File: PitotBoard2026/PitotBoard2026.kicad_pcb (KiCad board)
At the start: 2 copper layers, 50.2 x 41.5 mm, 65 parts, among them J1 RJ25, J2 ICSP(, J3 Conn_01x04_Socket, J4 Conn_01x04_Pin, J5 Conn_01x04_Socket, J6 Conn_01x04_Pin, SW1 RST, U1 ATmega328PB-A, U10 MCP25625-x-SS, U11 FXMA2102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

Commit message: Add files via upload
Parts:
- added ? (x2): , , F.Cu at (180.5, 141.7)
- added ? (x2): , , F.Cu at (180.5, 140.9)
- added ?: , , F.Cu at (145.9, 141.3)
- added ? (x2): , , F.Cu at (145.9, 139.7)
- added ?: , , F.Cu at (180.5, 142.5)
- added ? (x2): , , F.Cu at (145.9, 140.5)
- added G***: LOGO, KUBTSS:CYGNUS, F.Cu at (150.5, 140.1)
- added G***: LOGO, KUBTSS:Lba, F.Cu at (150.7, 137.1)
- added REF**: MountingHole_2.1mm, MountingHole:MountingHole_2.1mm, F.Cu at (145.9, 141.3)
- added REF**: MountingHole_2.1mm, MountingHole:MountingHole_2.1mm, F.Cu at (180.5, 142.5)
- moved J6 56.6 mm to (182.6, 137.0)
- moved C27 56.6 mm to (186.2, 139.9)
- moved U3 56.6 mm to (186.4, 142.4)
- moved C14 3.54 mm to (135.3, 134.5)
- moved J4 3.54 mm to (135.1, 129.0)
- moved C15 3.54 mm to (139.4, 139.1)
- moved REF** 3.54 mm to (143.3, 140.5)
- moved REF** 3.54 mm to (135.0, 140.5)
- moved U7 3.54 mm to (138.8, 134.6)
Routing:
- net GND2: track 26.9 -> 35.6 mm, vias 2 -> 8
- net GND: track 155.3 -> 159.5 mm, vias 35 -> 40
- net GND1: vias 3 -> 5
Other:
- board size 50.2 x 41.5 mm -> 59.7 x 40.2 mm

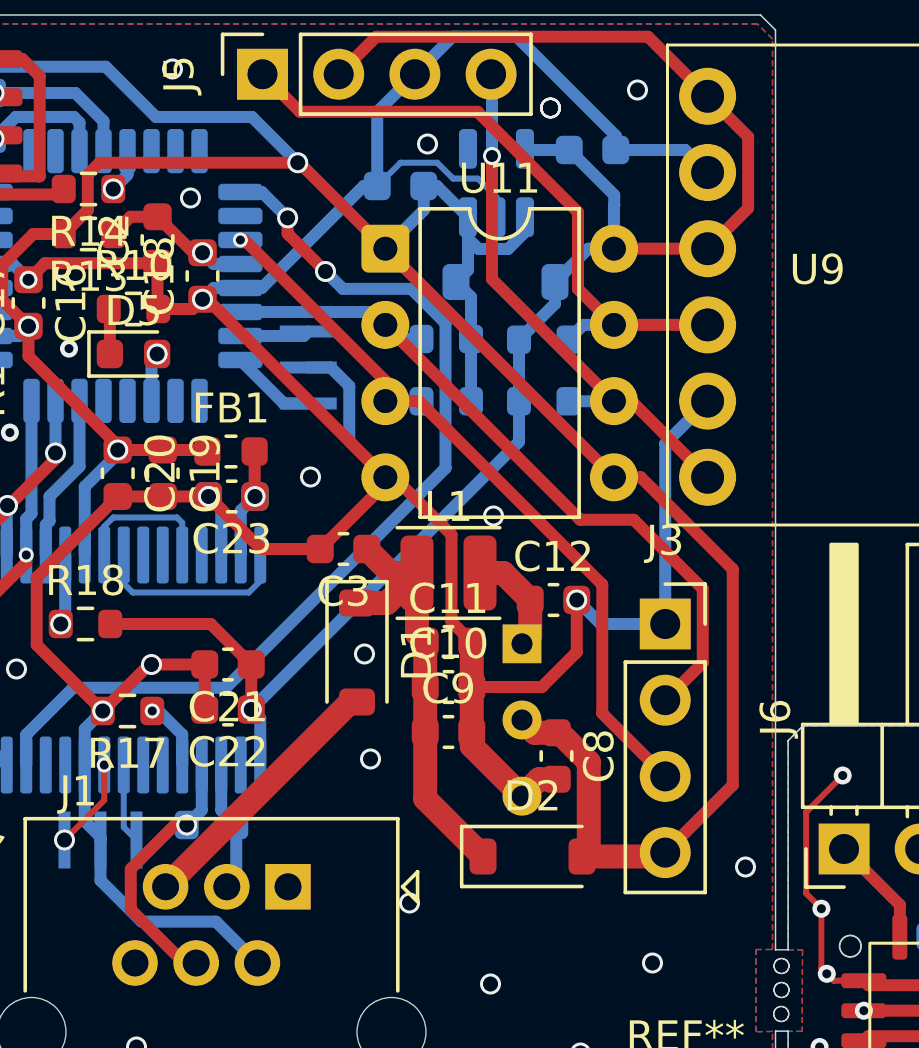
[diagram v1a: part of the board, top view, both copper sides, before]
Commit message: Add files via upload
FXMA2102とM78ARのフットプリントを修正
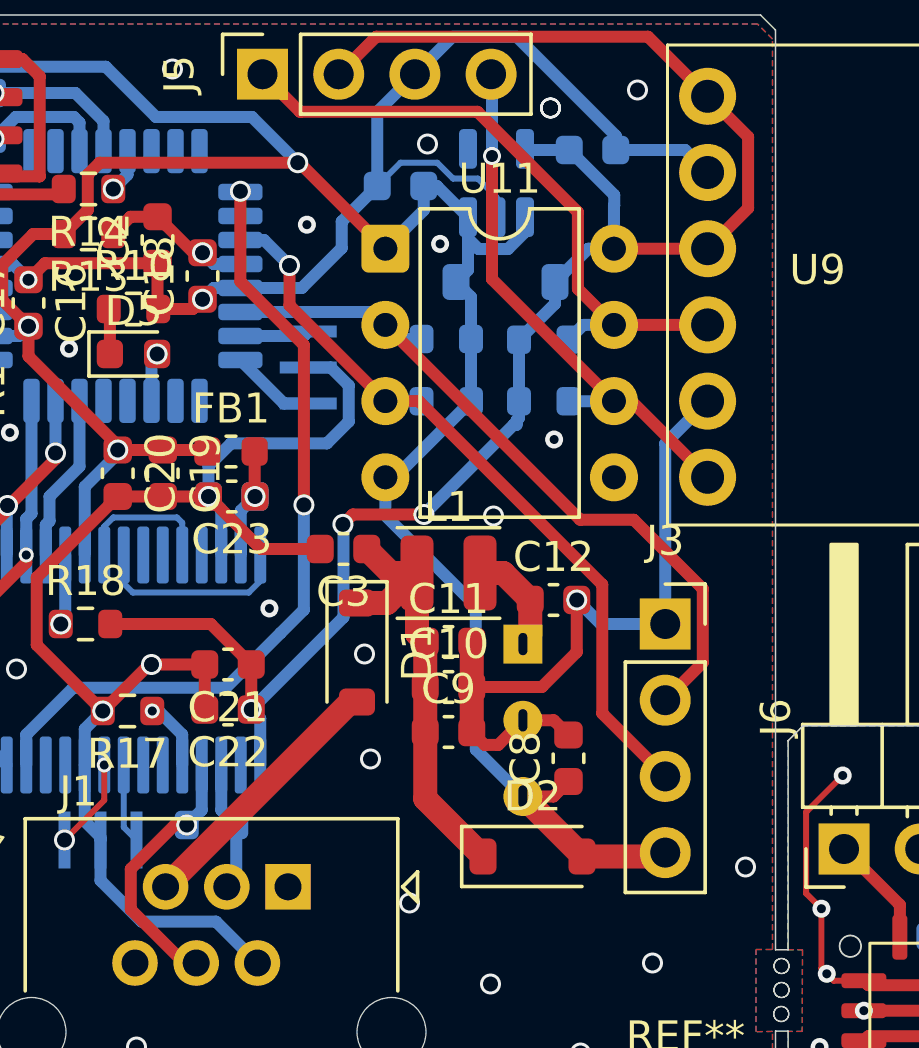
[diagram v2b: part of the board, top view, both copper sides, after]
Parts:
- J2: value ICSP( -> ICSP
- U2: footprint Package_SIP:SIP3_11.6x8.5mm -> KUBTSS:SIP3_11.6x8.5mm
- moved C8 0.41 mm to (173.4, 134.0), turned to 90 degrees
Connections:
- U11 pad 4: GND -> +5V
- U11 pad 5: +5V -> GND
- U2 pad 2: +5V -> GND
- U2 pad 3: GND -> +5V
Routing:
- net GND: track 159.5 -> 145.2 mm, vias 40 -> 42
- net +5V: track 126.5 -> 115.7 mm
- net INT: track 32.5 -> 26.8 mm
- net +3V3: track 58.0 -> 59.4 mm, vias 1 -> 3

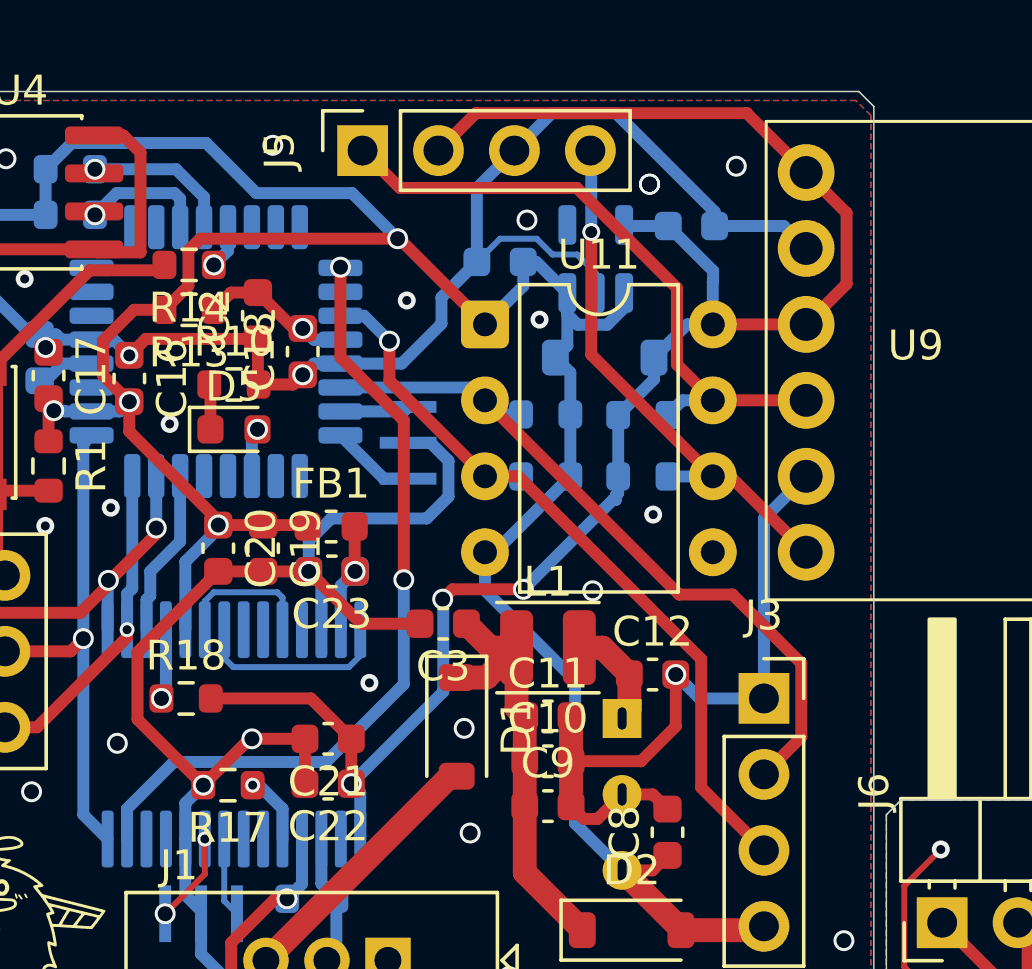
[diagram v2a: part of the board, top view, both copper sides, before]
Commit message: Add files via upload
MCP25625を5Vに変更。FXMA2102のピン番号を修正。
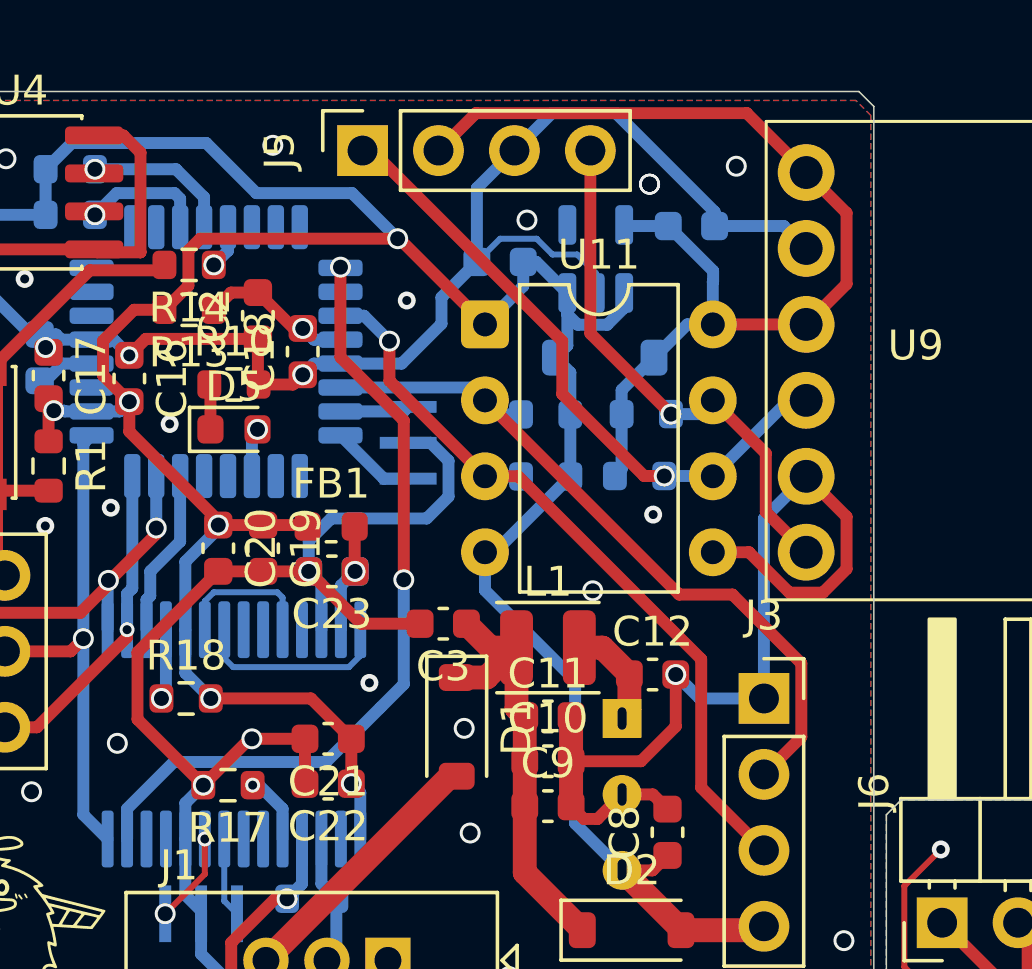
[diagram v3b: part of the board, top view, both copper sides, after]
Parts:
- moved R22 2.09 mm to (172.7, 120.0)
- moved R23 2.04 mm to (172.5, 122.1)
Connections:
- C21 pad 1: +3V3 -> +5V
- C22 pad 1: +3V3 -> +5V
- R18 pad 2: +3V3 -> +5V
- U10 pad 1: +3V3 -> +5V
- U11 pad 6: SCL3 -> SDA3
- U11 pad 7: SDA3 -> SCL3
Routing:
- net +3V3: track 59.4 -> 35.3 mm, vias 3 -> 0
- net +5V: track 115.7 -> 127.1 mm, vias 5 -> 7
- net GND: track 145.2 -> 154.2 mm, vias 42 -> 41
- net SDA3: track 21.5 -> 22.0 mm, vias 0 -> 1
